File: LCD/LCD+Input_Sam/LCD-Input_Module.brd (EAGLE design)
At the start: 100 x 65 mm, 23 parts

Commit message: LCD PCB final touches
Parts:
- JP2: device pinhead:1X03 -> pinhead:1X04
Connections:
- new net SA0: JP2.4, U$1.P$43
- net VDD: no longer U$1.P$43
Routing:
- net SA0: track 0.00 -> 12.4 mm
- net SCL: track 29.6 -> 32.3 mm
- net !RES: track 16.7 -> 17.6 mm
- net SDA: track 26.1 -> 26.9 mm
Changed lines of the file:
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@@
 <attribute name="VALUE" x="17.42" y="55.935" size="1.27" layer="27"/>
 </element>
-<element name="JP2" library="pinhead" library_urn="urn:adsk.eagle:library:325" package="1X03" package3d_urn="urn:adsk.eagle:package:22458/2" value="" x="51.83" y="59.11" smashed="yes">
+<element name="JP2" library="pinhead" library_urn="urn:adsk.eagle:library:325" package="1X04" package3d_urn="urn:adsk.eagle:package:22407/2" value="" x="51.83" y="59.11" smashed="yes">
 <attribute name="NAME" x="47.9438" y="60.9388" size="1.27" layer="25" ratio="10"/>
 <attribute name="POPULARITY" value="92" x="110.25" y="4.5" size="1.778" layer="27" display="off"/>
@@
 <contactref element="U$1" pad="P$39"/>
 <contactref element="R7" pad="2"/>
-<wire x1="49.29" y1="59.11" x2="49.29" y2="59" width="0.4" layer="1"/>
-<wire x1="49.29" y1="59" x2="49.29" y2="51.82" width="0.4" layer="1"/>
-<wire x1="49.29" y1="51.82" x2="51.07" y2="50.04" width="0.4" layer="1"/>
+<wire x1="48.02" y1="59.11" x2="40.24" y2="59.11" width="0.4" layer="1"/>
+<wire x1="40.24" y1="59.11" x2="40.13" y2="59" width="0.4" layer="1"/>
+<wire x1="40.13" y1="59" x2="38" y2="59" width="0.4" layer="1"/>
+<wire x1="51.07" y1="51.22" x2="51.07" y2="50.04" width="0.4" layer="1"/>
+<wire x1="51.07" y1="51.22" x2="43.29" y2="59" width="0.4" layer="1"/>
 <wire x1="53.61" y1="50.04" x2="51.07" y2="50.04" width="0.4" layer="1"/>
 <wire x1="36.1" y1="58.54" x2="37.54" y2="58.54" width="0.4" layer="16"/>
-<wire x1="37.54" y1="58.54" x2="38.5" y2="59.5" width="0.4" layer="1"/>
-<wire x1="38.5" y1="59.5" x2="48.79" y2="59.5" width="0.4" layer="1"/>
-<wire x1="48.79" y1="59.5" x2="49.29" y2="59" width="0.4" layer="1"/>
+<wire x1="37.54" y1="58.54" x2="38" y2="59" width="0.4" layer="1"/>
 <via x="37.54" y="58.54" extent="1-16" drill="0.35"/>
 </signal>
@@
 <contactref element="U$1" pad="P$1"/>
 <contactref element="U$1" pad="P$41"/>
-<contactref element="U$1" pad="P$43"/>
 <contactref element="U$1" pad="P$42"/>
 <contactref element="U$1" pad="P$33"/>
@@
 <contactref element="U$1" pad="P$37"/>
 <contactref element="R7" pad="1"/>
-<contactref element="R8" pad="1"/>
-<contactref element="R1" pad="2"/>
-<contactref element="R2" pad="2"/>
-<contactref element="R3" pad="2"/>
-<contactref element="R4" pad="2"/>
 <wire x1="12.97" y1="8.24" x2="35.87" y2="31.14" width="0.6" layer="1"/>
 <wire x1="35.87" y1="47.54" x2="38.37" y2="50.04" width="0.6" layer="1"/>
@@
 <wire x1="43.45" y1="50.04" x2="45.99" y2="50.04" width="0.6" layer="1"/>
 <wire x1="45.99" y1="50.04" x2="48.53" y2="50.04" width="0.6" layer="1"/>
-<wire x1="63.77" y1="50.04" x2="61.23" y2="50.04" width="0.6" layer="1"/>
 <wire x1="61.23" y1="50.04" x2="58.69" y2="50.04" width="0.6" layer="1"/>
 <wire x1="18.69" y1="59.11" x2="21.08" y2="61.5" width="0.6" layer="1"/>
-<wire x1="90.465" y1="43.58" x2="87.9633375" y2="43.58" width="0.6" layer="16"/>
-<wire x1="87.9633375" y1="43.58" x2="85.461675" y2="43.58" width="0.6" layer="16"/>
-<wire x1="85.461675" y1="43.58" x2="82.9600125" y2="43.58" width="0.6" layer="16"/>
-<wire x1="90.85" y1="63.15" x2="94" y2="60" width="0.6" layer="1"/>
-<wire x1="82.8800125" y1="43.5" x2="82.9600125" y2="43.58" width="0.6" layer="16"/>
-<wire x1="75.65" y1="63.15" x2="90.85" y2="63.15" width="0.6" layer="1"/>
-<wire x1="65.31" y1="48" x2="63.77" y2="49.54" width="0.6" layer="1"/>
-<wire x1="63.77" y1="50.04" x2="63.77" y2="49.54" width="0.6" layer="1"/>
-<wire x1="69" y1="48" x2="65.31" y2="48" width="0.6" layer="1"/>
 <wire x1="55.22666875" y1="47.1478" x2="55.25386875" y2="47.175" width="0.6" layer="1"/>
 <wire x1="50.99333125" y1="47.1478" x2="48.53" y2="49.61113125" width="0.6" layer="1"/>
@@
 <wire x1="34.84" y1="61.5" x2="36.1" y2="60.24" width="0.6" layer="16"/>
 <wire x1="21.08" y1="61.5" x2="34.84" y2="61.5" width="0.6" layer="1"/>
+<via x="34.84" y="61.5" extent="1-16" drill="0.35"/>
+<contactref element="R4" pad="2"/>
+<wire x1="82.8800125" y1="43.5" x2="82.9600125" y2="43.58" width="0.6" layer="16"/>
+<contactref element="R3" pad="2"/>
+<wire x1="85.461675" y1="43.58" x2="82.9600125" y2="43.58" width="0.6" layer="16"/>
+<contactref element="R2" pad="2"/>
+<wire x1="87.9633375" y1="43.58" x2="85.461675" y2="43.58" width="0.6" layer="16"/>
+<contactref element="R1" pad="2"/>
+<wire x1="90.465" y1="43.58" x2="87.9633375" y2="43.58" width="0.6" layer="16"/>
+<wire x1="91.965" y1="43.58" x2="90.465" y2="43.58" width="0.6" layer="16"/>
+<via x="91.965" y="43.58" extent="1-16" drill="0.35"/>
+<wire x1="94" y1="45.615" x2="91.965" y2="43.58" width="0.6" layer="1"/>
+<wire x1="94" y1="60" x2="94" y2="45.615" width="0.6" layer="1"/>
+<wire x1="90.85" y1="63.15" x2="94" y2="60" width="0.6" layer="1"/>
+<wire x1="75.65" y1="63.15" x2="90.85" y2="63.15" width="0.6" layer="1"/>
+<via x="75.65" y="63.15" extent="1-16" drill="0.35"/>
+<wire x1="75.65" y1="63.15" x2="71.26" y2="58.76" width="0.6" layer="16"/>
+<contactref element="R8" pad="1"/>
+<wire x1="69.76" y1="58.76" x2="71.26" y2="58.76" width="0.6" layer="16"/>
+<wire x1="69.76" y1="58.76" x2="68.26" y2="57.26" width="0.6" layer="16"/>
 <wire x1="68.26" y1="57.26" x2="68.26" y2="51.26" width="0.6" layer="16"/>
 <wire x1="68.26" y1="51.26" x2="69.76" y2="49.76" width="0.6" layer="16"/>
-<wire x1="69.76" y1="58.76" x2="68.26" y2="57.26" width="0.6" layer="16"/>
-<wire x1="69.76" y1="49.76" x2="69.76" y2="48.76" width="0.6" layer="1"/>
-<wire x1="69.76" y1="48.76" x2="69" y2="48" width="0.6" layer="1"/>
-<wire x1="69.76" y1="58.76" x2="71.26" y2="58.76" width="0.6" layer="16"/>
-<wire x1="75.65" y1="63.15" x2="71.26" y2="58.76" width="0.6" layer="16"/>
-<wire x1="94" y1="60" x2="94" y2="45.615" width="0.6" layer="1"/>
-<wire x1="94" y1="45.615" x2="91.965" y2="43.58" width="0.6" layer="1"/>
-<wire x1="91.965" y1="43.58" x2="90.465" y2="43.58" width="0.6" layer="16"/>
-<via x="91.965" y="43.58" extent="1-16" drill="0.35"/>
-<via x="34.84" y="61.5" extent="1-16" drill="0.35"/>
 <via x="69.76" y="49.76" extent="1-16" drill="0.35"/>
-<via x="75.65" y="63.15" extent="1-16" drill="0.35"/>
+<wire x1="69.76" y1="49.76" x2="68.76" y2="49.76" width="0.6096" layer="1"/>
+<wire x1="68.76" y1="49.76" x2="66.5" y2="47.5" width="0.6096" layer="1"/>
+<wire x1="66.5" y1="47.5" x2="63.77" y2="47.5" width="0.6096" layer="1"/>
+<wire x1="63.77" y1="47.5" x2="61.23" y2="50.04" width="0.6096" layer="1"/>
 </signal>
 <signal name="!RES">
 <contactref element="JP2" pad="3"/>
 <contactref element="U$1" pad="P$44"/>
-<wire x1="54.37" y1="59.11" x2="58.98" y2="54.5" width="0.4" layer="1"/>
-<wire x1="58.98" y1="54.5" x2="63.5" y2="54.5" width="0.4" layer="1"/>
+<wire x1="53.1" y1="59.11" x2="58.98" y2="54.5" width="0.4" layer="1"/>
+<wire x1="58.98" y1="54.5" x2="61.5" y2="54.5" width="0.4" layer="1"/>
+<wire x1="61.5" y1="54.5" x2="63.5" y2="54.5" width="0.4" layer="1"/>
 <wire x1="63.5" y1="54.5" x2="66.31" y2="51.69" width="0.4" layer="1"/>
 <wire x1="66.31" y1="51.69" x2="66.31" y2="50.04" width="0.4" layer="1"/>
@@
 <contactref element="R8" pad="2"/>
 <contactref element="U$1" pad="P$40"/>
-<wire x1="51.83" y1="59.11" x2="51.83" y2="56.17" width="0.4" layer="1"/>
+<wire x1="50.56" y1="59.11" x2="51.83" y2="56.17" width="0.4" layer="1"/>
 <wire x1="56.15" y1="51.85" x2="56.15" y2="50.04" width="0.4" layer="1"/>
 <wire x1="51.83" y1="56.17" x2="56.15" y2="51.85" width="0.4" layer="1"/>
-<wire x1="51.83" y1="59.11" x2="52.032" y2="59.11" width="0.4" layer="1"/>
-<wire x1="52.032" y1="59.11" x2="53.9084" y2="60.9864" width="0.4" layer="1"/>
-<wire x1="57.9864" y1="60.9864" x2="58" y2="61" width="0.4" layer="1"/>
-<wire x1="53.9084" y1="60.9864" x2="57.9864" y2="60.9864" width="0.4" layer="1"/>
-<wire x1="58" y1="61" x2="67.78" y2="61" width="0.4" layer="1"/>
+<wire x1="52.922" y1="62" x2="50.56" y2="59.638" width="0.4" layer="1"/>
+<wire x1="50.56" y1="59.11" x2="50.56" y2="59.638" width="0.4" layer="1"/>
+<wire x1="66.78" y1="62" x2="67.78" y2="61" width="0.4" layer="1"/>
+<wire x1="66.78" y1="62" x2="59" y2="62" width="0.4" layer="1"/>
+<wire x1="59" y1="62" x2="52.922" y2="62" width="0.4" layer="1"/>
 <wire x1="67.78" y1="61" x2="69.76" y2="60.46" width="0.4" layer="16"/>
 <via x="67.78" y="61" extent="1-16" drill="0.35"/>
@@
 <wire x1="83" y1="59.06" x2="83" y2="53" width="0.4064" layer="1"/>
 </signal>
+<signal name="SA0">
+<contactref element="JP2" pad="4"/>
+<contactref element="U$1" pad="P$43"/>
+<wire x1="55.64" y1="59.11" x2="63.77" y2="50.98" width="0.4064" layer="16"/>
+<wire x1="63.77" y1="50.98" x2="63.77" y2="50.04" width="0.4064" layer="16"/>
+</signal>
 </signals>

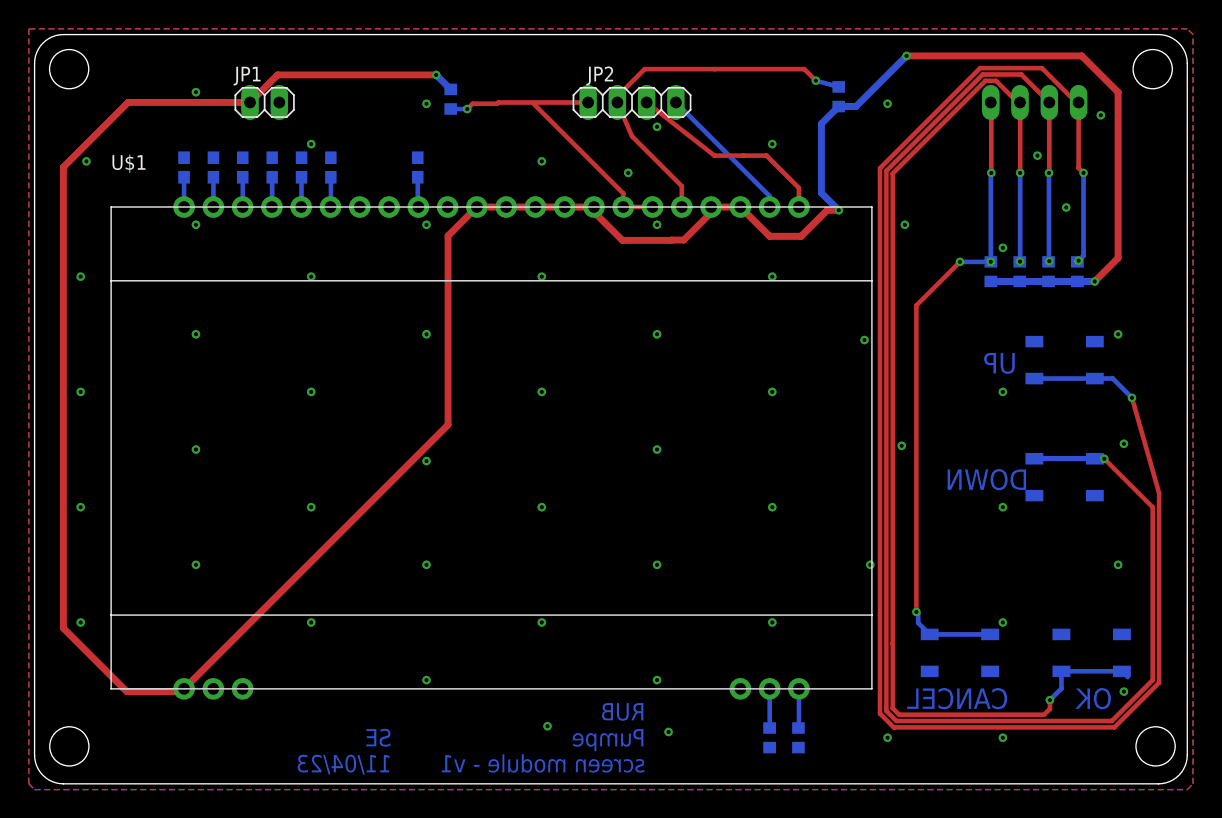
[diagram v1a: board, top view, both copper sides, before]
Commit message: LCD PCB changes according to Robins suggestions. Still pending one thing
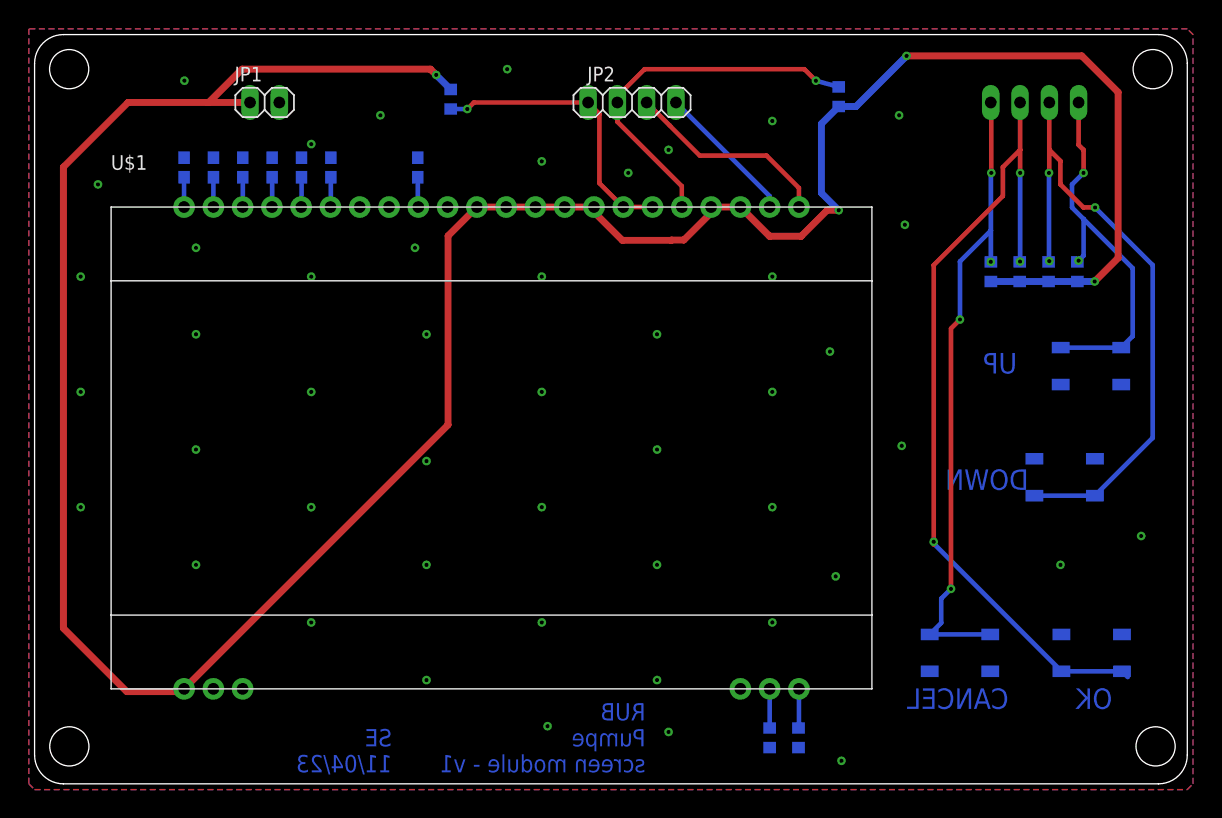
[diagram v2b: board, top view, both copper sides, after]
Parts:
- moved S1-UP 2.34 mm to (91.6, 36.2), turned to 180 degrees
- turned S2-DOWN to 0 degrees
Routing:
- net UP: track 144.3 -> 34.0 mm, vias 3 -> 2
- net DOWN: track 136.5 -> 55.5 mm
- net OK: track 99.1 -> 73.2 mm
- net VDD: track 242.9 -> 247.0 mm
- net SDA: track 26.9 -> 25.0 mm
- net N$10: track 2.60 -> 2.54 mm, vias 1 -> 0
- net N$9: track 2.60 -> 2.55 mm, vias 1 -> 0
- net N$5: track 2.59 -> 2.55 mm, vias 1 -> 0
- net N$7: track 2.59 -> 2.56 mm, vias 1 -> 0
- net N$6: track 2.59 -> 2.57 mm, vias 1 -> 0
- net N$4: track 2.58 -> 2.57 mm, vias 1 -> 0

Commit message: LCD PCB finished (again)
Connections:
- removed net N$10: C1.1, U$1.P$31
- net VDD: now also C1.1, U$1.P$31
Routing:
- net VDD: track 247.0 -> 255.4 mm, vias 4 -> 5
- net N$10: track 2.54 -> 0.00 mm
- net OK: track 73.2 -> 72.0 mm, vias 3 -> 2
- net UP: track 34.0 -> 33.6 mm, vias 2 -> 1
- net DOWN: vias 3 -> 2
- net CANCEL: vias 4 -> 3
